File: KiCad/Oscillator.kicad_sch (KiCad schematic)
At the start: 36 parts, among them Q1 NPN, Q2 PNP, Q3 NPN, Q4 PNP, U2 40106, U3 TL074

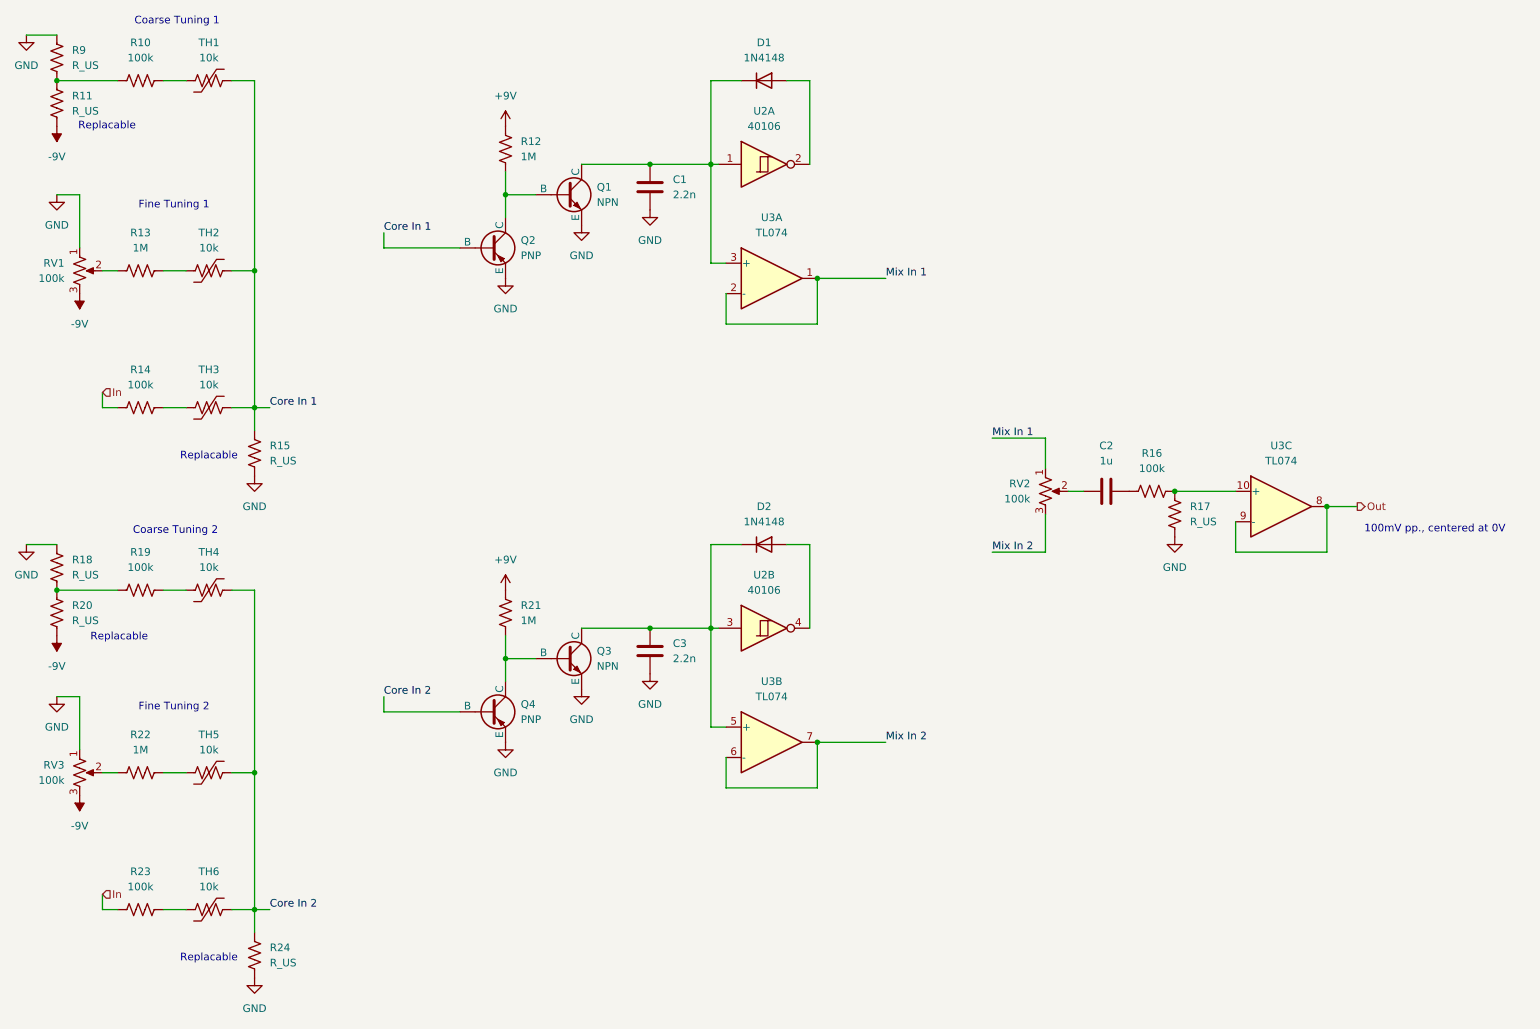
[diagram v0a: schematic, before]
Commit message: updated footprints
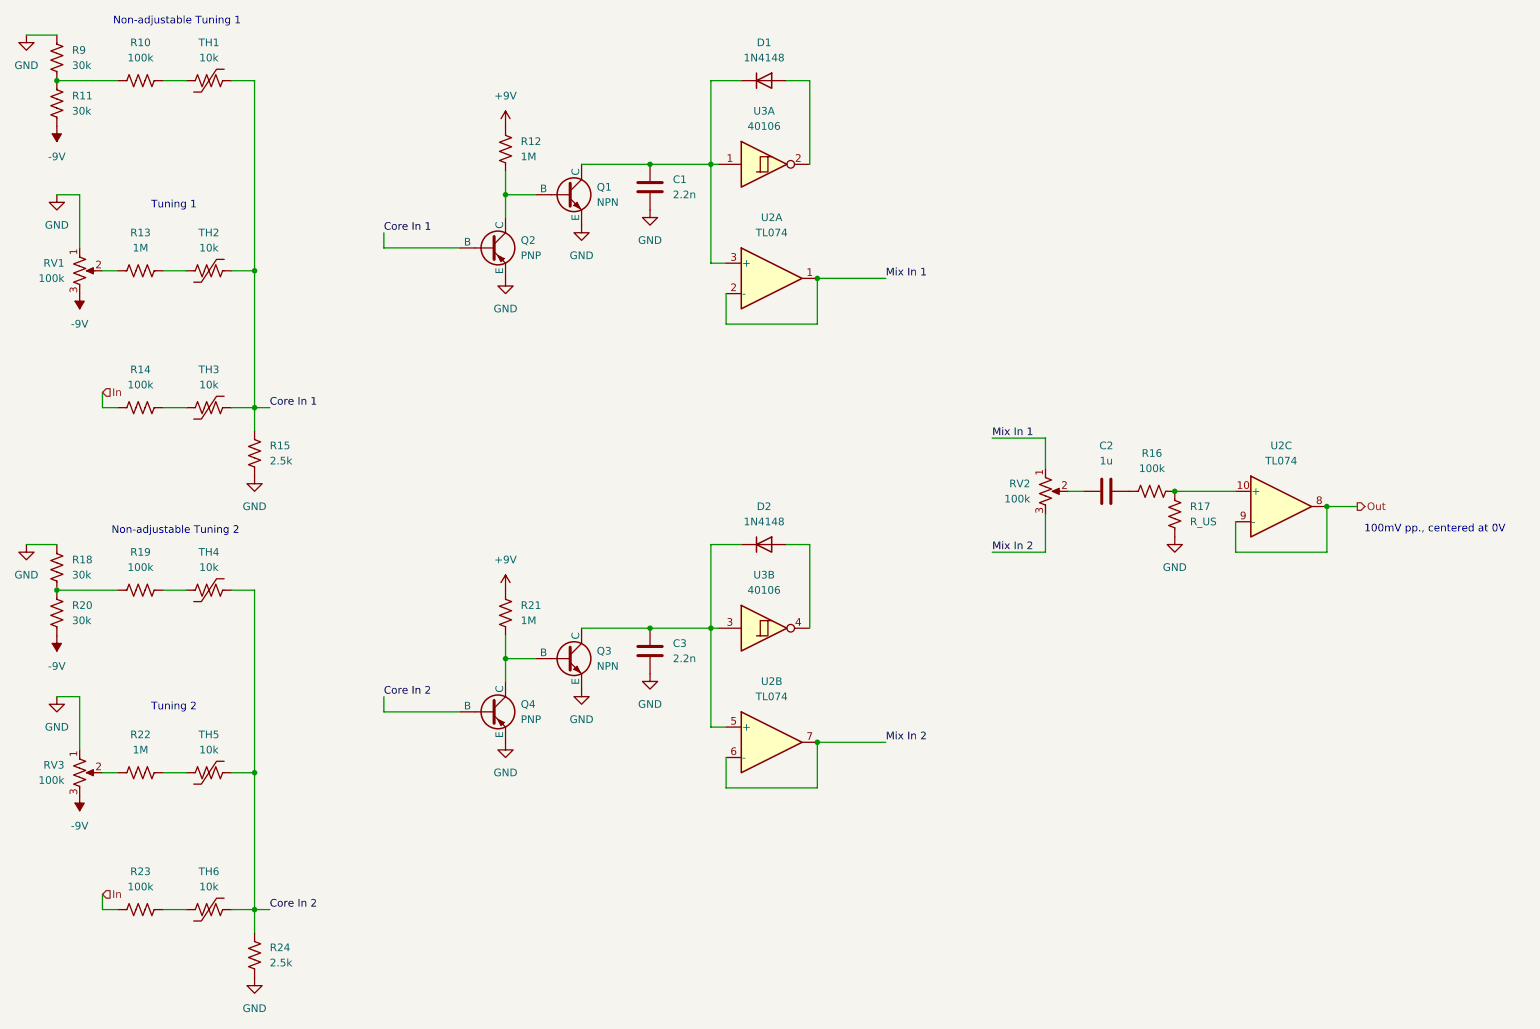
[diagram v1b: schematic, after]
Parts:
- C2: footprint Capacitor_THT:C_Rect_L7.5mm_W6.5mm_P5.00mm -> Capacitor_THT:C_Rect_L7.2mm_W4.5mm_P5.00mm
- R11, R18, R20, R9: value R_US -> 30k
- R15, R24: value R_US -> 2.5k; footprint (none) -> Resistor_SMD:R_0603_1608Metric
- R17: footprint Resistor_SMD:R_0201_0603Metric -> Resistor_THT:R_Axial_DIN0207_L6.3mm_D2.5mm_P7.62mm_Horizontal
- TH1, TH2, TH3, TH4, TH5, TH6: footprint Resistor_SMD:R_0201_0603Metric -> Resistor_THT:R_Radial_Power_L12.0mm_W8.0mm_P5.00mm
- U2: renamed from U3; footprint Op Amp TL074CD:SOIC_074CD_STM -> Package_DIP:DIP-14_W7.62mm
- renumbered U2 to U3
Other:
- note added: "Non-adjustable Tuning 1"
- note added: "Non-adjustable Tuning 2"
- note added: "Tuning 1"
- note added: "Tuning 2"
- note removed: "Coarse Tuning 1"
- note removed: "Coarse Tuning 2"
- note removed: "Fine Tuning 1"
- note removed: "Fine Tuning 2"
- note removed: "Replacable"

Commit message: added potentiometer voltage control cct
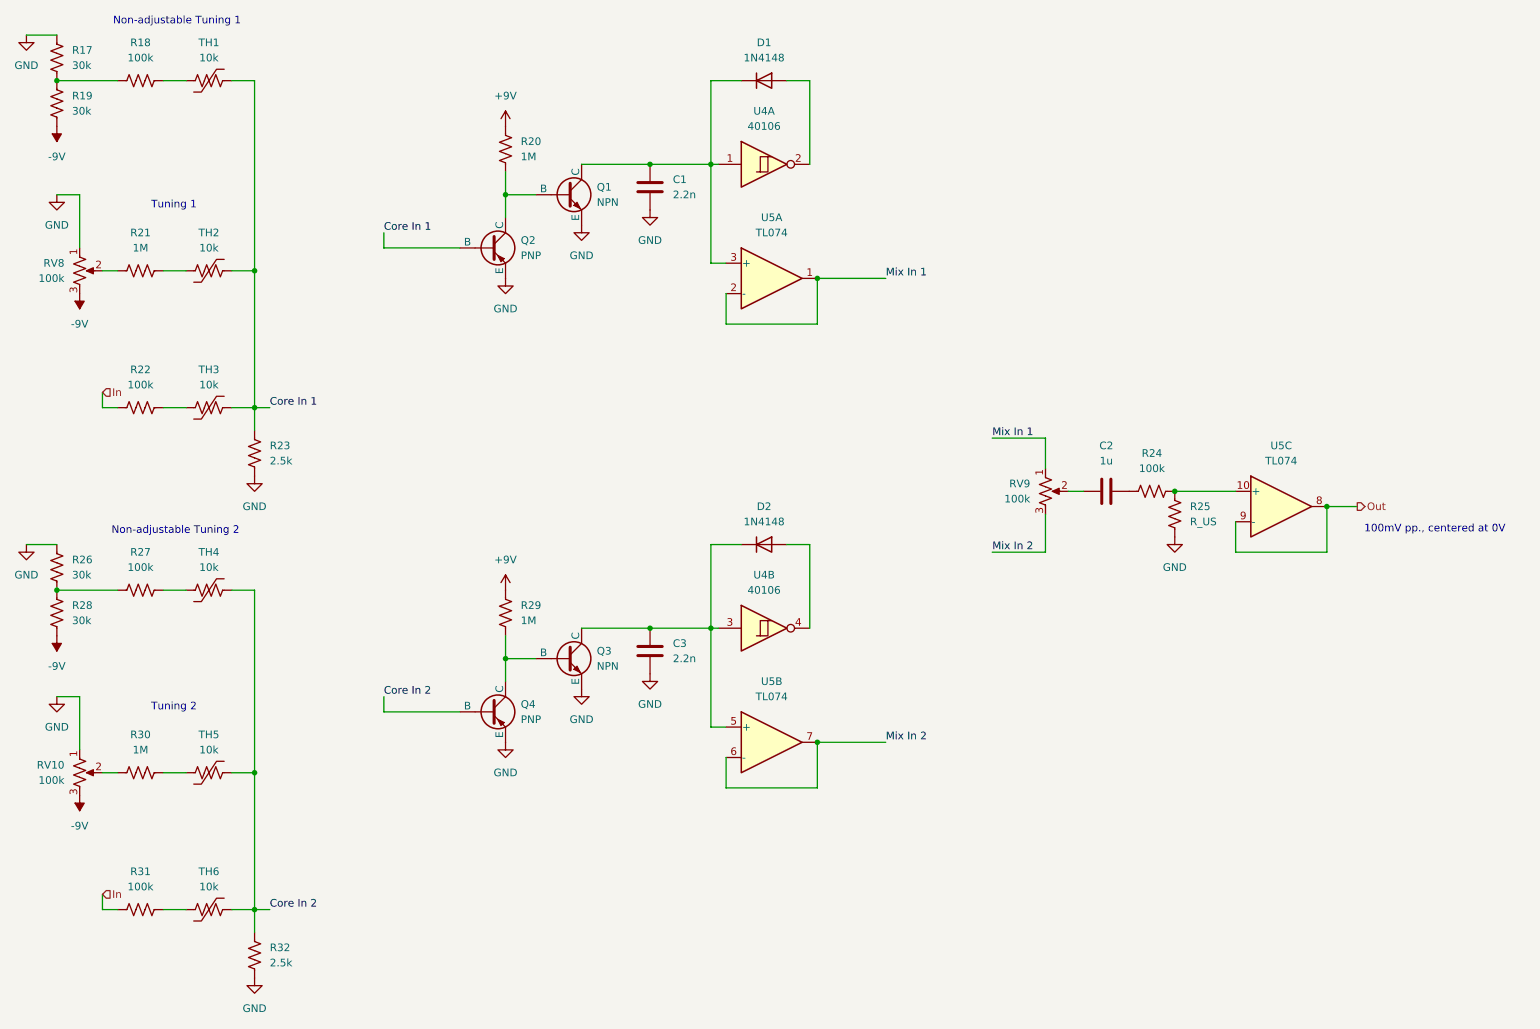
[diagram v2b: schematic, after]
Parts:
- renumbered R9 to R17, R10 to R18, R11 to R19, R12 to R20, R13 to R21, R14 to R22, R15 to R23, R16 to R24, R17 to R25, R18 to R26, R19 to R27, R20 to R28, R21 to R29, R22 to R30, R23 to R31, R24 to R32, RV3 to RV10, RV1 to RV8, RV2 to RV9, U3 to U4, U2 to U5

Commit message: added volume control knob
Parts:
- renumbered RV9 to RV10, RV10 to RV11, RV8 to RV9
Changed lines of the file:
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@@
 		(dnp no)
 		(fields_autoplaced yes)
-		(property "Reference" "#PWR040"
+		(property "Reference" "#PWR041"
 			(at 105.41 78.74 0)
 			(hide yes)
@@
 			(project "Electronic Trombone"
 				(path "/931827f3-33b7-460f-8885-7db258da2648/c601a773-7a8a-4dbf-b4ab-ef5ea2e44138"
-					(reference "#PWR040")
+					(reference "#PWR041")
 					(unit 1)
 				)
@@
 		(dnp no)
 		(fields_autoplaced yes)
-		(property "Reference" "#PWR046"
+		(property "Reference" "#PWR047"
 			(at 30.48 128.27 0)
 			(hide yes)
@@
 			(project "Electronic Trombone"
 				(path "/931827f3-33b7-460f-8885-7db258da2648/c601a773-7a8a-4dbf-b4ab-ef5ea2e44138"
-					(reference "#PWR046")
+					(reference "#PWR047")
 					(unit 1)
 				)
@@
 		(dnp no)
 		(fields_autoplaced yes)
-		(property "Reference" "#PWR044"
+		(property "Reference" "#PWR045"
 			(at 25.4 123.19 0)
 			(hide yes)
@@
 			(project "Electronic Trombone"
 				(path "/931827f3-33b7-460f-8885-7db258da2648/c601a773-7a8a-4dbf-b4ab-ef5ea2e44138"
-					(reference "#PWR044")
+					(reference "#PWR045")
 					(unit 1)
 				)
@@
 		(dnp no)
 		(fields_autoplaced yes)
-		(property "Reference" "#PWR042"
+		(property "Reference" "#PWR043"
 			(at 63.5 111.76 0)
 			(hide yes)
@@
 			(project "Electronic Trombone"
 				(path "/931827f3-33b7-460f-8885-7db258da2648/c601a773-7a8a-4dbf-b4ab-ef5ea2e44138"
-					(reference "#PWR042")
+					(reference "#PWR043")
 					(unit 1)
 				)
@@
 		(dnp no)
 		(fields_autoplaced yes)
-		(property "Reference" "#PWR036"
+		(property "Reference" "#PWR037"
 			(at 105.41 50.8 0)
 			(hide yes)
@@
 			(project "Electronic Trombone"
 				(path "/931827f3-33b7-460f-8885-7db258da2648/c601a773-7a8a-4dbf-b4ab-ef5ea2e44138"
-					(reference "#PWR036")
+					(reference "#PWR037")
 					(unit 1)
 				)
@@
 		(dnp no)
 		(fields_autoplaced yes)
-		(property "Reference" "#PWR045"
+		(property "Reference" "#PWR046"
 			(at 105.41 128.27 0)
 			(hide yes)
@@
 			(project "Electronic Trombone"
 				(path "/931827f3-33b7-460f-8885-7db258da2648/c601a773-7a8a-4dbf-b4ab-ef5ea2e44138"
-					(reference "#PWR045")
+					(reference "#PWR046")
 					(unit 1)
 				)
@@
 		(dnp no)
 		(fields_autoplaced yes)
-		(property "Reference" "#PWR035"
+		(property "Reference" "#PWR036"
 			(at 30.48 43.18 0)
 			(hide yes)
@@
 			(project "Electronic Trombone"
 				(path "/931827f3-33b7-460f-8885-7db258da2648/c601a773-7a8a-4dbf-b4ab-ef5ea2e44138"
-					(reference "#PWR035")
+					(reference "#PWR036")
 					(unit 1)
 				)
@@
 		(dnp no)
 		(fields_autoplaced yes)
-		(property "Reference" "#PWR043"
+		(property "Reference" "#PWR044"
 			(at 217.17 121.92 0)
 			(hide yes)
@@
 			(project "Electronic Trombone"
 				(path "/931827f3-33b7-460f-8885-7db258da2648/c601a773-7a8a-4dbf-b4ab-ef5ea2e44138"
-					(reference "#PWR043")
+					(reference "#PWR044")
 					(unit 1)
 				)
@@
 		(dnp no)
 		(fields_autoplaced yes)
-		(property "Reference" "#PWR050"
+		(property "Reference" "#PWR051"
 			(at 105.41 156.21 0)
 			(hide yes)
@@
 			(project "Electronic Trombone"
 				(path "/931827f3-33b7-460f-8885-7db258da2648/c601a773-7a8a-4dbf-b4ab-ef5ea2e44138"
-					(reference "#PWR050")
+					(reference "#PWR051")
 					(unit 1)
 				)
@@
 		(dnp no)
 		(fields_autoplaced yes)
-		(property "Reference" "#PWR049"
+		(property "Reference" "#PWR050"
 			(at 30.48 148.59 0)
 			(hide yes)
@@
 			(project "Electronic Trombone"
 				(path "/931827f3-33b7-460f-8885-7db258da2648/c601a773-7a8a-4dbf-b4ab-ef5ea2e44138"
-					(reference "#PWR049")
+					(reference "#PWR050")
 					(unit 1)
 				)
@@
 		(dnp no)
 		(fields_autoplaced yes)
-		(property "Reference" "#PWR039"
+		(property "Reference" "#PWR040"
 			(at 118.11 69.85 0)
 			(hide yes)
@@
 			(project "Electronic Trombone"
 				(path "/931827f3-33b7-460f-8885-7db258da2648/c601a773-7a8a-4dbf-b4ab-ef5ea2e44138"
-					(reference "#PWR039")
+					(reference "#PWR040")
 					(unit 1)
 				)
@@
 		(dnp no)
 		(fields_autoplaced yes)
-		(property "Reference" "#PWR052"
+		(property "Reference" "#PWR053"
 			(at 63.5 195.58 0)
 			(hide yes)
@@
 			(project "Electronic Trombone"
 				(path "/931827f3-33b7-460f-8885-7db258da2648/c601a773-7a8a-4dbf-b4ab-ef5ea2e44138"
-					(reference "#PWR052")
+					(reference "#PWR053")
 					(unit 1)
 				)
@@
 		(dnp no)
 		(fields_autoplaced yes)
-		(property "Reference" "#PWR051"
+		(property "Reference" "#PWR052"
 			(at 34.29 154.94 0)
 			(hide yes)
@@
 			(project "Electronic Trombone"
 				(path "/931827f3-33b7-460f-8885-7db258da2648/c601a773-7a8a-4dbf-b4ab-ef5ea2e44138"
-					(reference "#PWR051")
+					(reference "#PWR052")
 					(unit 1)
 				)
@@
 		(dnp no)
 		(fields_autoplaced yes)
-		(property "Reference" "RV10"
+		(property "Reference" "RV11"
 			(at 31.75 153.6699 0)
 			(show_name no)
@@
 			(project "Electronic Trombone"
 				(path "/931827f3-33b7-460f-8885-7db258da2648/c601a773-7a8a-4dbf-b4ab-ef5ea2e44138"
-					(reference "RV10")
+					(reference "RV11")
 					(unit 1)
 				)
@@
 		(dnp no)
 		(fields_autoplaced yes)
-		(property "Reference" "#PWR038"
+		(property "Reference" "#PWR039"
 			(at 129.54 67.31 0)
 			(hide yes)
@@
 			(project "Electronic Trombone"
 				(path "/931827f3-33b7-460f-8885-7db258da2648/c601a773-7a8a-4dbf-b4ab-ef5ea2e44138"
-					(reference "#PWR038")
+					(reference "#PWR039")
 					(unit 1)
 				)
@@
 		(dnp no)
 		(fields_autoplaced yes)
-		(property "Reference" "#PWR047"
+		(property "Reference" "#PWR048"
 			(at 129.54 144.78 0)
 			(hide yes)
@@
 			(project "Electronic Trombone"
 				(path "/931827f3-33b7-460f-8885-7db258da2648/c601a773-7a8a-4dbf-b4ab-ef5ea2e44138"
-					(reference "#PWR047")
+					(reference "#PWR048")
 					(unit 1)
 				)
@@
 		(dnp no)
 		(fields_autoplaced yes)
-		(property "Reference" "RV8"
+		(property "Reference" "RV9"
 			(at 31.75 69.8499 0)
 			(show_name no)
@@
 			(project "Electronic Trombone"
 				(path "/931827f3-33b7-460f-8885-7db258da2648/c601a773-7a8a-4dbf-b4ab-ef5ea2e44138"
-					(reference "RV8")
+					(reference "RV9")
 					(unit 1)
 				)
@@
 		(dnp no)
 		(fields_autoplaced yes)
-		(property "Reference" "RV9"
+		(property "Reference" "RV10"
 			(at 193.04 106.6799 0)
 			(show_name no)
@@
 			(project "Electronic Trombone"
 				(path "/931827f3-33b7-460f-8885-7db258da2648/c601a773-7a8a-4dbf-b4ab-ef5ea2e44138"
-					(reference "RV9")
+					(reference "RV10")
 					(unit 1)
 				)
@@
 		(dnp no)
 		(fields_autoplaced yes)
-		(property "Reference" "#PWR034"
+		(property "Reference" "#PWR035"
 			(at 25.4 38.1 0)
 			(hide yes)
@@
 			(project "Electronic Trombone"
 				(path "/931827f3-33b7-460f-8885-7db258da2648/c601a773-7a8a-4dbf-b4ab-ef5ea2e44138"
-					(reference "#PWR034")
+					(reference "#PWR035")
 					(unit 1)
 				)
@@
 		(dnp no)
 		(fields_autoplaced yes)
-		(property "Reference" "#PWR048"
+		(property "Reference" "#PWR049"
 			(at 118.11 147.32 0)
 			(hide yes)
@@
 			(project "Electronic Trombone"
 				(path "/931827f3-33b7-460f-8885-7db258da2648/c601a773-7a8a-4dbf-b4ab-ef5ea2e44138"
-					(reference "#PWR048")
+					(reference "#PWR049")
 					(unit 1)
 				)
@@
 		(dnp no)
 		(fields_autoplaced yes)
-		(property "Reference" "#PWR037"
+		(property "Reference" "#PWR038"
 			(at 30.48 64.77 0)
 			(hide yes)
@@
 			(project "Electronic Trombone"
 				(path "/931827f3-33b7-460f-8885-7db258da2648/c601a773-7a8a-4dbf-b4ab-ef5ea2e44138"
-					(reference "#PWR037")
+					(reference "#PWR038")
 					(unit 1)
 				)
@@
 		(dnp no)
 		(fields_autoplaced yes)
-		(property "Reference" "#PWR041"
+		(property "Reference" "#PWR042"
 			(at 34.29 71.12 0)
 			(hide yes)
@@
 			(project "Electronic Trombone"
 				(path "/931827f3-33b7-460f-8885-7db258da2648/c601a773-7a8a-4dbf-b4ab-ef5ea2e44138"
-					(reference "#PWR041")
+					(reference "#PWR042")
 					(unit 1)
 				)
